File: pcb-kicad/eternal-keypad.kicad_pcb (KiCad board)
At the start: 2 copper layers, 169.9 x 95.3 mm, 80 parts

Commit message: Publish v1.1
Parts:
- removed ?: , 
- removed REF** (x2): MountingHole_4.6mm_Pad_Via, MountingHole:MountingHole_4.6mm_Pad_Via_Custom
- added LED1: WS2812B, * duckyb-collection:LED_WS2812B_PLCC4_5.0x5.0mm_P3.2mm, F.Cu at (68.3, 114.3)
- added LED2: WS2812B, * duckyb-collection:LED_WS2812B_PLCC4_5.0x5.0mm_P3.2mm, F.Cu at (148.4, 114.3)
- added LED3: WS2812B, * duckyb-collection:LED_WS2812B_PLCC4_5.0x5.0mm_P3.2mm, F.Cu at (207.2, 114.3)
- added LED4: WS2812B, * duckyb-collection:LED_WS2812B_PLCC4_5.0x5.0mm_P3.2mm, F.Cu at (185.7, 93.7)
- added LED5: WS2812B, * duckyb-collection:LED_WS2812B_PLCC4_5.0x5.0mm_P3.2mm, F.Cu at (207.2, 57.1)
- added LED6: WS2812B, * duckyb-collection:LED_WS2812B_PLCC4_5.0x5.0mm_P3.2mm, F.Cu at (147.6, 56.4)
- added LED7: WS2812B, * duckyb-collection:LED_WS2812B_PLCC4_5.0x5.0mm_P3.2mm, F.Cu at (84.9, 57.1)
- added LED8: WS2812B, * duckyb-collection:LED_WS2812B_PLCC4_5.0x5.0mm_P3.2mm, F.Cu at (96.8, 93.7)
- added STAB1: Stabilizer_MX_2u, Keyswitches by Daprice:Stabilizer_MX_2u, F.Cu at (172.2, 125.4)
- added Standoff 1: MountingHole_4.6mm_Pad_Via, MountingHole:MountingHole_3.2mm_M3_Pad_Via, F.Cu at (102.4, 58.7)
- added Standoff 4: MountingHole_4.6mm_Pad_Via, MountingHole:MountingHole_3.2mm_M3_Pad_Via, F.Cu at (79.4, 115.9)
- D1, D10, D11, D12, D13, D14, D15, D16, D17, D18, D19, D2, D20, D21, D22, D23, D24, D25, D26, D27, D28, D29, D3, D30, D31, D32, D33, D34, D35, D36, D4, D5, D6, D7, D8, D9: footprint Diode_THT:D_DO-35_SOD27_P7.62mm_Horizontal_Reversible -> * duckyb-collection:D_SMD_TH
- MX1, MX16, MX24, MX32, MX33, MX8: footprint MX_Only:MXOnly-1.25U-Reversible-NoLED -> * duckyb-collection:MX_socket_reversible
- MX10, MX11, MX12, MX13, MX14, MX15, MX17, MX18, MX19, MX2, MX20, MX21, MX22, MX23, MX25, MX26, MX27, MX28, MX29, MX3, MX30, MX31, MX34, MX36, MX4, MX5, MX6, MX7, MX9: footprint MX_Only:MXOnly-1U-Reversible-NoLED -> * duckyb-collection:MX_socket_reversible
- MX35: footprint MX_Only:MXOnly-2.75U-Reversible-ReversedStabilizers-NoLED -> * duckyb-collection:MX_socket_reversible
- ProMicro1: renamed from FACE DOWN; value ProMicro-Reversible-NoLabels -> ProMicro; footprint promicro:ProMicro-Reversible-NoLabels -> Promicro-Jumpers:ProMicro_facedown
- Standoff 2: renamed from REF**; footprint MountingHole:MountingHole_4.6mm_Pad_Via_Custom -> MountingHole:MountingHole_3.2mm_M3_Pad_Via
- Standoff 3: renamed from REF**; footprint MountingHole:MountingHole_4.6mm_Pad_Via_Custom -> MountingHole:MountingHole_3.2mm_M3_Pad_Via
- moved D33 5.32 mm to (105.6, 124.6)
- moved D11 4.83 mm to (141.3, 67.5)
- moved D15 4.83 mm to (73.0, 86.5)
- moved D23 4.83 mm to (73.0, 105.6)
- moved D31 4.83 mm to (73.0, 124.6)
- moved D35 4.83 mm to (153.2, 124.6)
- moved D10 4.76 mm to (122.2, 67.5)
- moved D12 4.76 mm to (160.3, 67.5)
- moved D13 4.76 mm to (179.4, 67.5)
- moved D14 4.76 mm to (198.4, 67.5)
- moved D16 4.76 mm to (81.8, 86.5)
- moved D17 4.76 mm to (103.2, 86.5)
- moved D18 4.76 mm to (122.2, 86.5)
- moved D19 4.76 mm to (141.3, 86.5)
- moved D20 4.76 mm to (160.3, 86.5)
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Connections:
- ProMicro1 pad 1: Net-(ProMicro1-Pad1) -> RGB
- ProMicro1 pad 2: Net-(ProMicro1-Pad2) -> unconnected-(ProMicro1-Pad2)
- ProMicro1 pad 22: Net-(ProMicro1-Pad22) -> unconnected-(ProMicro1-Pad22)
- ProMicro1 pad 24: Net-(ProMicro1-Pad24) -> unconnected-(ProMicro1-Pad24)
- ProMicro1 pad 5: Net-(ProMicro1-Pad5) -> unconnected-(ProMicro1-Pad5)
- ProMicro1 pad 6: Net-(ProMicro1-Pad6) -> unconnected-(ProMicro1-Pad6)
- ProMicro1 pad 7: Net-(ProMicro1-Pad7) -> unconnected-(ProMicro1-Pad7)
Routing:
- net VCC: track 18.8 -> 385.0 mm, vias 0 -> 13
- net RGB: track 0.00 -> 88.7 mm, vias 0 -> 1
- net Net-(LED1-Pad2): track 0.00 -> 88.4 mm, vias 0 -> 2
- net Net-(LED4-Pad2): track 0.00 -> 80.5 mm, vias 0 -> 2
- net Net-(LED6-Pad2): track 0.00 -> 75.1 mm, vias 0 -> 2
- net Net-(LED5-Pad2): track 0.00 -> 72.7 mm, vias 0 -> 2
- net Net-(LED2-Pad2): track 0.00 -> 66.8 mm, vias 0 -> 2
- net Net-(LED7-Pad2): track 0.00 -> 52.4 mm, vias 0 -> 3
- net Net-(LED3-Pad2): track 0.00 -> 49.6 mm, vias 0 -> 2
- net COL7: track 272.2 -> 227.2 mm, vias 0 -> 2
- net COL5: track 238.1 -> 194.6 mm
- net COL2: track 185.4 -> 142.9 mm
- net COL3: track 203.6 -> 161.2 mm
- net COL0: track 93.6 -> 51.2 mm
- net COL6: track 226.9 -> 191.5 mm, vias 0 -> 1
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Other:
- board size 169.9 x 95.3 mm -> 169.9 x 95.2 mm
- net class Default removed
- net class Power removed
- board text added: "1) Place Pro-Micro with components facing DOWN 2) Close JUMPER PADS on the OPPOSITE SIDE"
- board text added: "V1.1"
- board text removed: "V1.0"

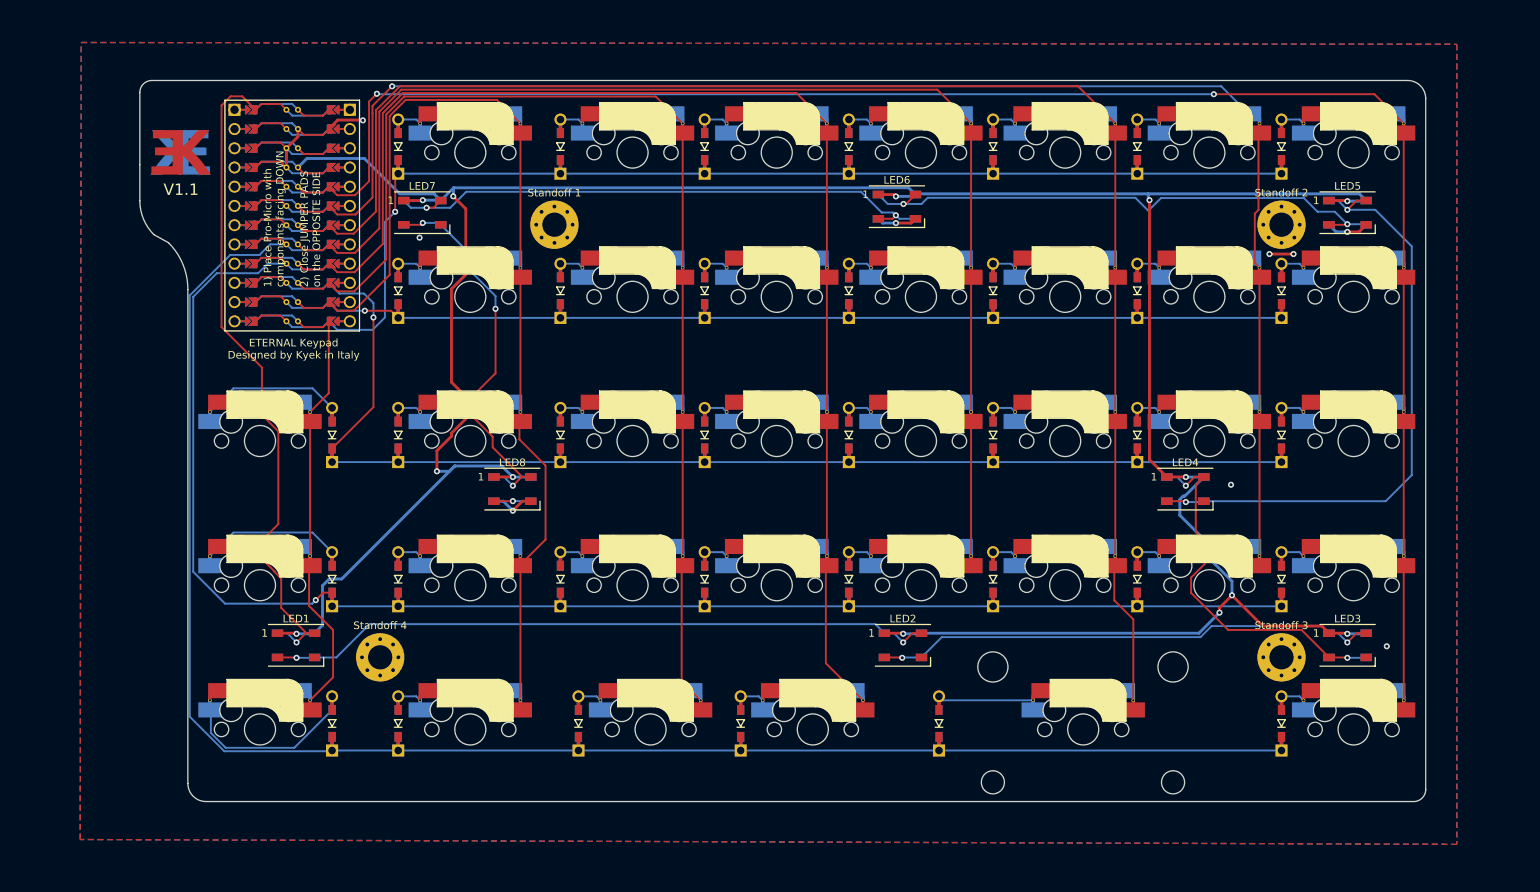
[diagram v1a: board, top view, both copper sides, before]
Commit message: Add power, reset, RGB Cutoff, Battery Pads
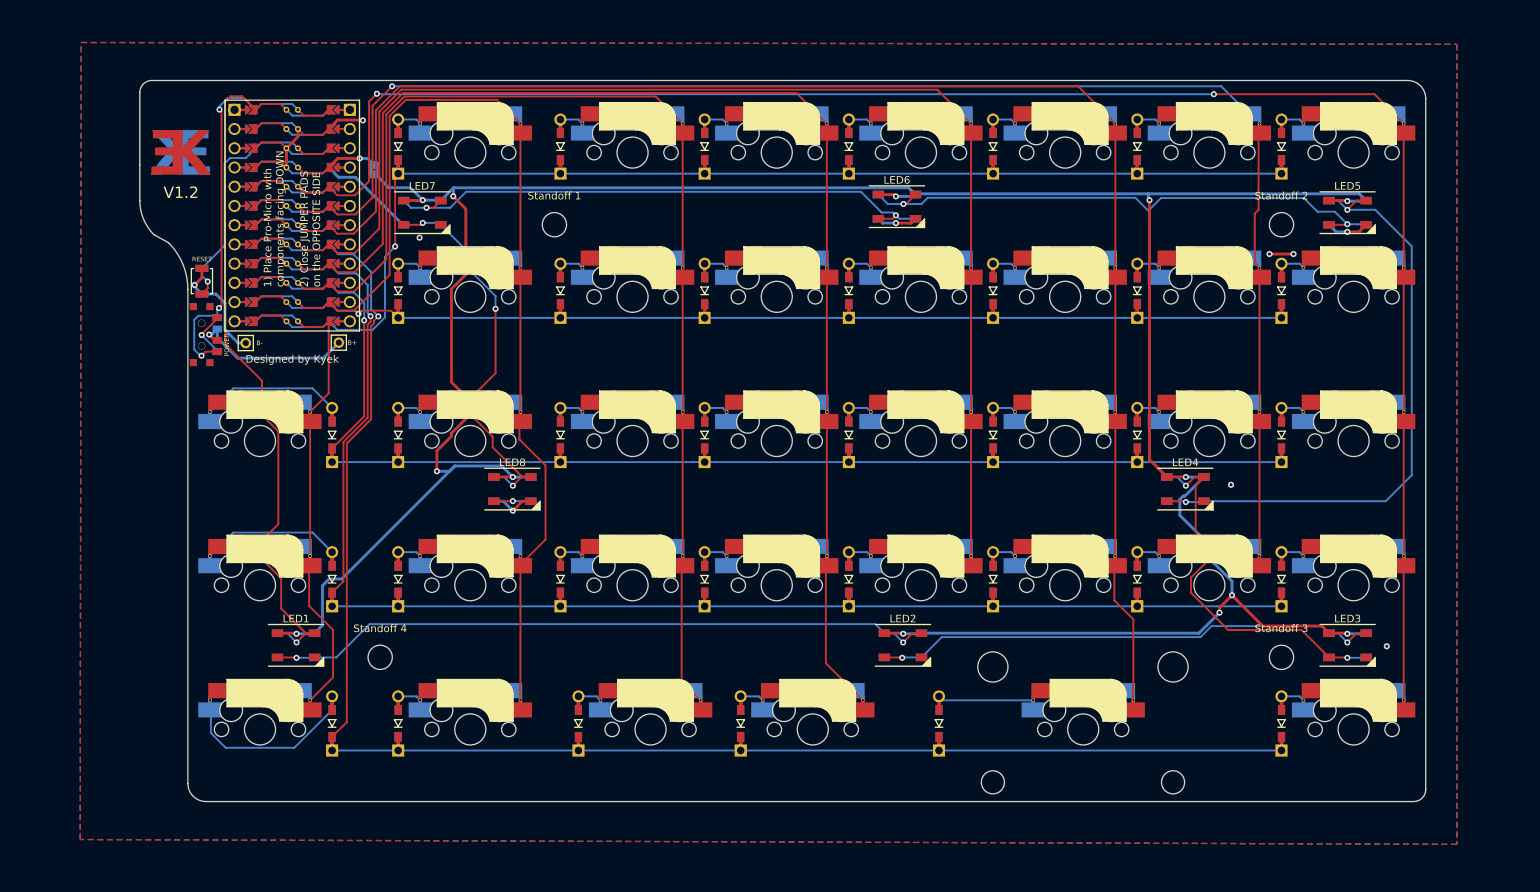
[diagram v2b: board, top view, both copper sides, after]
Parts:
- added Batt+1: MountingHole_Pad, * duckyb-collection:1pin_conn, F.Cu at (73.9, 74.3)
- added Batt-1: MountingHole_Pad, * duckyb-collection:1pin_conn, F.Cu at (61.6, 74.4)
- added JP1: Jumper_2_Bridged, Jumper:SolderJumper-2_P1.3mm_Bridged2Bar_RoundedPad1.0x1.5mm, B.Cu at (78.5, 51.5)
- added POWER1: SW_SPDT, * duckyb-collection:SPDT_C128955, F.Cu at (55.8, 73.3)
- added RSW1: SW_Push, * duckyb-collection:Tactile-Switch_SMT, F.Cu at (55.8, 66.2)
- Standoff 1: footprint MountingHole:MountingHole_3.2mm_M3_Pad_Via -> MountingHole:MountingHole_3.2mm_M3_DIN965
- Standoff 2: footprint MountingHole:MountingHole_3.2mm_M3_Pad_Via -> MountingHole:MountingHole_3.2mm_M3_DIN965
- Standoff 3: footprint MountingHole:MountingHole_3.2mm_M3_Pad_Via -> MountingHole:MountingHole_3.2mm_M3_DIN965
- Standoff 4: footprint MountingHole:MountingHole_3.2mm_M3_Pad_Via -> MountingHole:MountingHole_3.2mm_M3_DIN965
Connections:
- LED1 pad 1: VCC -> RGB VCC
- LED2 pad 1: VCC -> RGB VCC
- LED3 pad 1: VCC -> RGB VCC
- LED4 pad 1: VCC -> RGB VCC
- LED5 pad 1: VCC -> RGB VCC
- LED6 pad 1: VCC -> RGB VCC
- LED7 pad 1: VCC -> RGB VCC
- LED8 pad 1: VCC -> RGB VCC
- ProMicro1 pad 22: unconnected-(ProMicro1-Pad22) -> RST
- ProMicro1 pad 24: unconnected-(ProMicro1-Pad24) -> RAW
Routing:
- net VCC: track 385.0 -> 6.79 mm, vias 13 -> 1
- net RGB VCC: track 0.00 -> 371.3 mm, vias 0 -> 13
- net RAW: track 0.00 -> 45.0 mm, vias 0 -> 3
- net GND: track 30.9 -> 58.7 mm, vias 9 -> 10
- net RST: track 0.00 -> 24.1 mm, vias 0 -> 1
- net ROW3: track 196.5 -> 174.6 mm
- net B+: track 0.00 -> 21.9 mm, vias 0 -> 1
- net ROW4: track 217.4 -> 196.9 mm, vias 0 -> 1
- net unconnected-(POWER1-Pad1): track 0.00 -> 6.21 mm, vias 0 -> 1
- net ROW2: track 153.9 -> 152.2 mm
- net RGB: track 88.7 -> 87.2 mm
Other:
- board text added: "Designed by Kyek"
- board text added: "POWER"
- board text added: "RESET"
- board text added: "V1.2"
- board text removed: "ETERNAL Keypad Designed by Kyek in Italy"
- board text removed: "V1.1"
